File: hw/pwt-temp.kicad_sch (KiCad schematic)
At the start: 26 parts

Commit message: Flash hinzugefügt
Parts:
- added C?: 100nF, 00_pwt-temp_lib:C_0603, symbol Device:C_Small
- added J? (x2): CON_PH_2.54MM_2x3_VERT, 00_pwt-temp_lib:CON_PH_2.54MM_2x3_VERT, symbol 00_pwt-temp_lib:CON_PH_2.54MM_2x3_VERT
- added R?: 10k, symbol Device:R_Small
- added R?: 1k, symbol Device:R_Small
- added U?: IC_W25Q16JV, 00_pwt-temp_lib:IC_W25Q16JV, symbol 00_pwt-temp_lib:IC_W25Q16JV
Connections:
- net +3V3: now also C?.1, J?.2, J?.2, J?.3, J?.3, R?.1, U?.8 (VCC)
- net GND: now also C?.2, J?.4, J?.4, J?.5, J?.5, U?.4 (GND)
- net ~{BOOT}: now reaches U?.2 (GPIO0)
- net ~{BOOT}: now also R?.2
- net SPI_SD3: now reaches U?.51 (QSPI_SD3)
- net SPI_SD3: now also U?.7 (~{HD}/~{RST}(IO3))
- net SPI_SCLK: now reaches U?.52 (QSPI_SCLK)
- net SPI_SCLK: now also U?.6 (CLK)
- net SPI_SD0: now reaches U?.53 (QSPI_SD0)
- net SPI_SD0: now also U?.5 (DI(IO0))
- net SPI_SD2: now reaches U?.54 (QSPI_SD2)
- net SPI_SD2: now also U?.3 (~{WP}(IO2))
- net SPI_SD1: now reaches U?.55 (QSPI_SD1)
- net SPI_SD1: now also U?.2 (DO(IO1))
- net SPI_~{CS}: now reaches U?.56 (QSPI_SS_N)
- net SPI_~{CS}: now also R?.1, R?.2, U?.1 (~{CS})
- new net I2C_SCL: J?.6, J?.6
- new net I2C_SDA: J?.1, J?.1
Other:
- moved on the sheet: C?, R?, U?, Y?

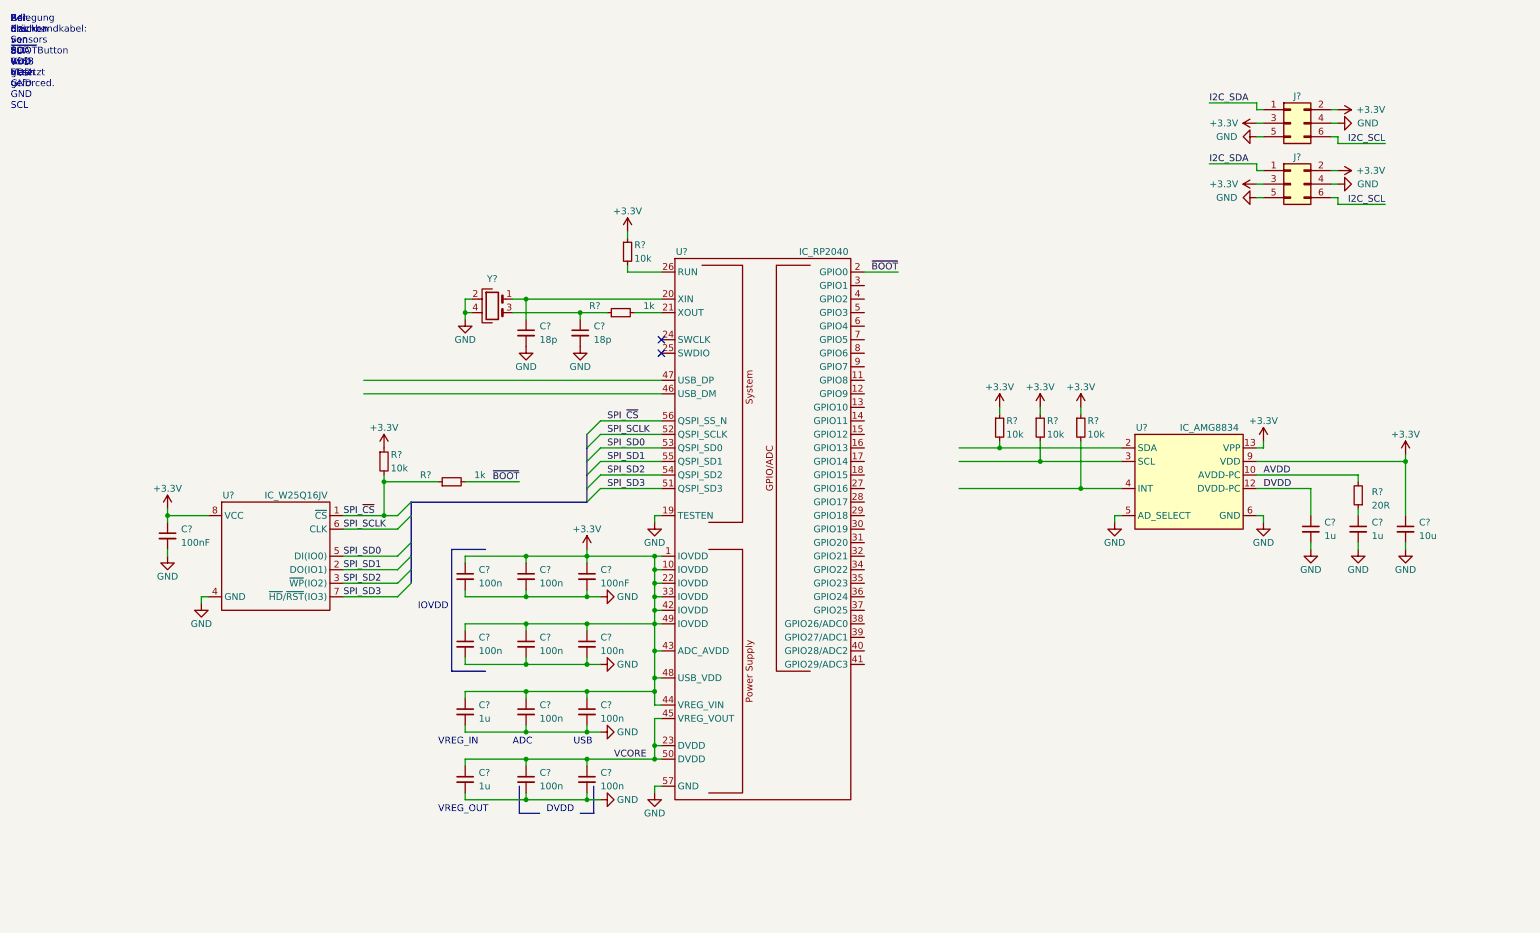
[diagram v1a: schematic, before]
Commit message: Boot Button hinzugefügt
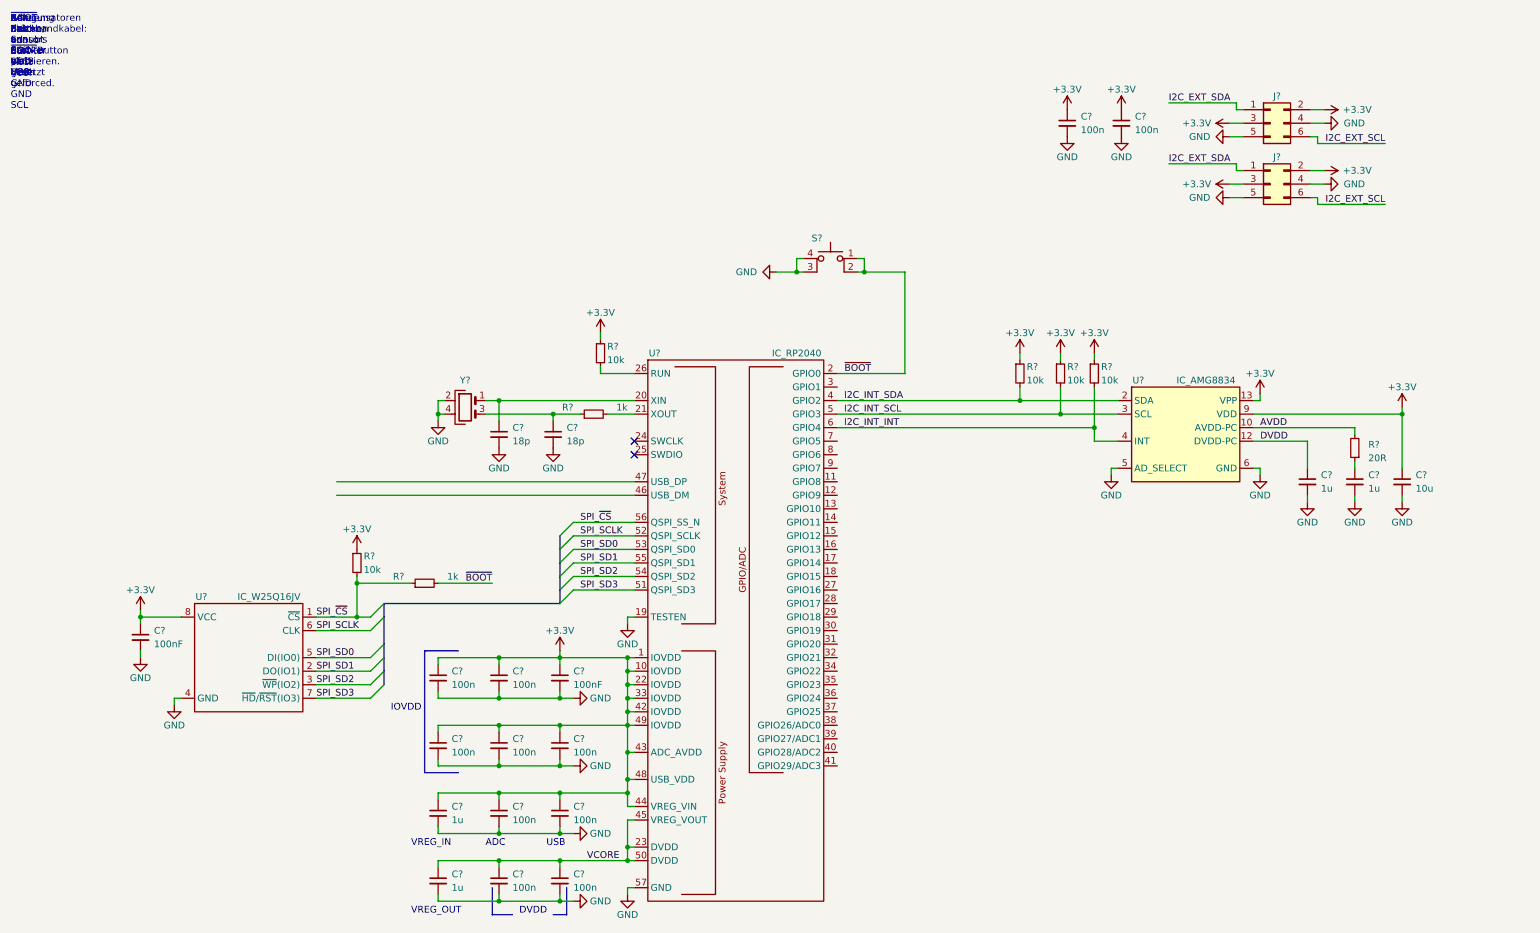
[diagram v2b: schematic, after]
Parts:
- removed J?: CON_PH_2.54MM_2x3_VERT, 00_pwt-temp_lib:CON_PH_2.54MM_2x3_VERT, symbol 00_pwt-temp_lib:CON_PH_2.54MM_2x3_VERT
- added C? (x2): 100n, 00_pwt-temp_lib:C_0603, symbol Device:C_Small
- added J?: CON_PH_2.54MM_2x3_VERT, 00_pwt-temp_lib:CON_PH_2.54MM_2x3_VERT, symbol 00_pwt-temp_lib:CON_PH_2.54MM_2x3_VERT
- added S?: MECH_BTN_SMD_SMALL, 00_pwt-temp_lib:MECH_BTN_SMD_SMALL, symbol 00_pwt-temp_lib:MECH_BTN_SMD_SMALL
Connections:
- net +3V3: now also C?.1, C?.1, J?.2, J?.3
- net GND: now also C?.2, C?.2, J?.4, J?.5, S?.3, S?.4
- net ~{BOOT}: now also S?.1, S?.2
- net I2C_INT_INT: now reaches R?.2, U?.4 (INT)
- net I2C_INT_INT: now also U?.6 (GPIO4)
- net I2C_INT_SCL: now reaches R?.2, U?.3 (SCL)
- net I2C_INT_SCL: now also U?.5 (GPIO3)
- net I2C_INT_SDA: now reaches R?.2, U?.2 (SDA)
- net I2C_INT_SDA: now also U?.4 (GPIO2)
- net I2C_SCL renamed I2C_EXT_SCL
- net I2C_EXT_SCL: now also J?.6
- net I2C_SDA renamed I2C_EXT_SDA
- net I2C_EXT_SDA: now also J?.1
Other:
- moved on the sheet: C?, J?, R?, U?, Y?

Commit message: Schaltplan Messplatine fertig
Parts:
- added C2, C3: 1u, 00_pwt-temp_lib:C_0603, symbol Device:C_Small
- added D1: D_SCH_40V_0.25A, 00_pwt-temp_lib:SOD_323, symbol 00_pwt-temp_lib:D_SCH_40V_0.25A
- added H1, H2, H3, H4: MountingHole_Pad, MountingHole:MountingHole_3.2mm_M3_Pad_Via, symbol Mechanical:MountingHole_Pad
- added J1: CON_USB_B_MINI, 00_pwt-temp_lib:CON_USB_B_MINI, symbol 00_pwt-temp_lib:CON_USB_B_MINI
- added R2, R3: 27.4R, 00_pwt-temp_lib:R_0603, symbol Device:R_Small
- added U1: PMIC_LDO_3V3_0.2A, 00_pwt-temp_lib:SOT_23_3, symbol 00_pwt-temp_lib:PMIC_LDO_3V3_0.2A
- R1, R10, R4, R5, R6, R7, R8, R9: renamed from R?; footprint (none) -> 00_pwt-temp_lib:R_0603
- gave numbers to parts that had none: 27
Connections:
- net +3V3: now also C3.1, U1.2 (OUT)
- net GND: now also C2.2, C3.2, H1.1, H2.1, H3.1, H4.1, J1.5 (GND), U1.1 (GND)
- net at U3.46 (USB_DM): now also R3.2
- net at U3.47 (USB_DP): now also R2.2
- new net: C2.1, D1.1 (K), U1.3 (IN)
- new net USB_DN: J1.2 (D-), R3.1
- new net USB_DP: J1.3 (D+), R2.1
- new net VBUS: D1.2 (A), J1.1 (VBUS)
- no-connect marks 2 -> 4
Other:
- moved on the sheet: C1, C10, C11, C12, C13, C14, C15, C16, C17, C18, C19, C20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
